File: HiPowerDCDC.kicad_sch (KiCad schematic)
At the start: 69 parts, among them J1 Conn_01x01, J2 Conn_01x01, J3 Conn_01x01, J4 Conn_01x01, J5 Conn_01x04, J6 Conn_01x02, Q1 WMJ38N60, Q2 WMJ38N60, SW1 SW_Push, SW2 SW_Push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

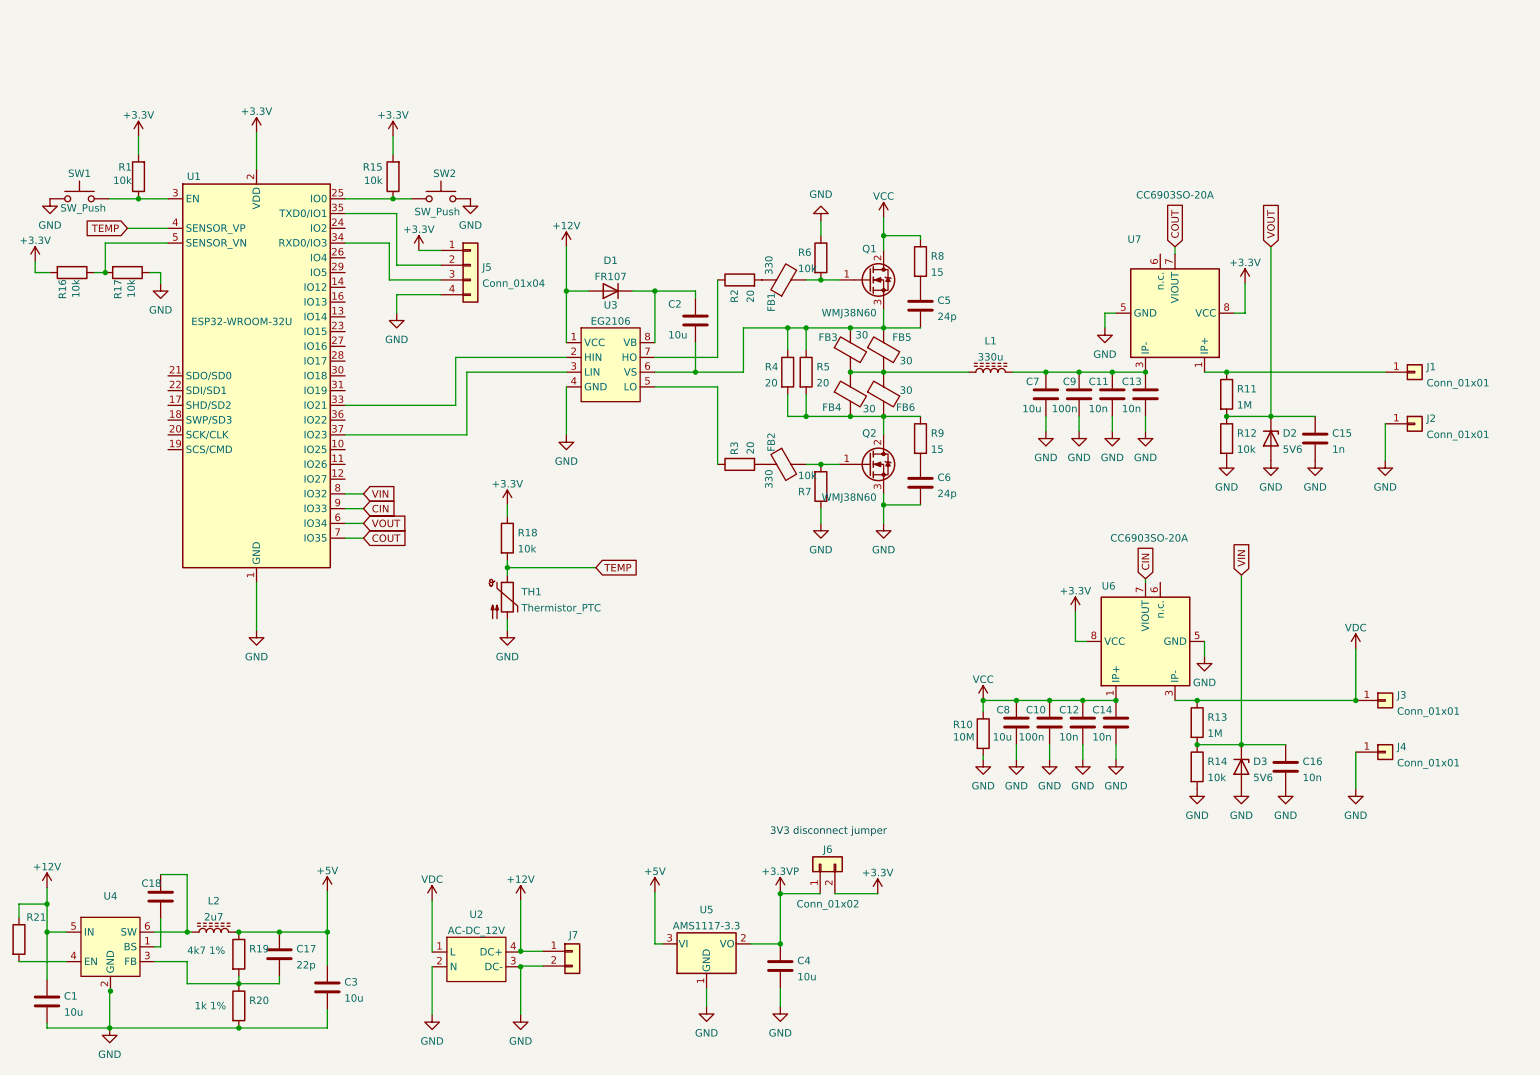
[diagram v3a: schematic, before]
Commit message: Increased DCDC inductor footprint
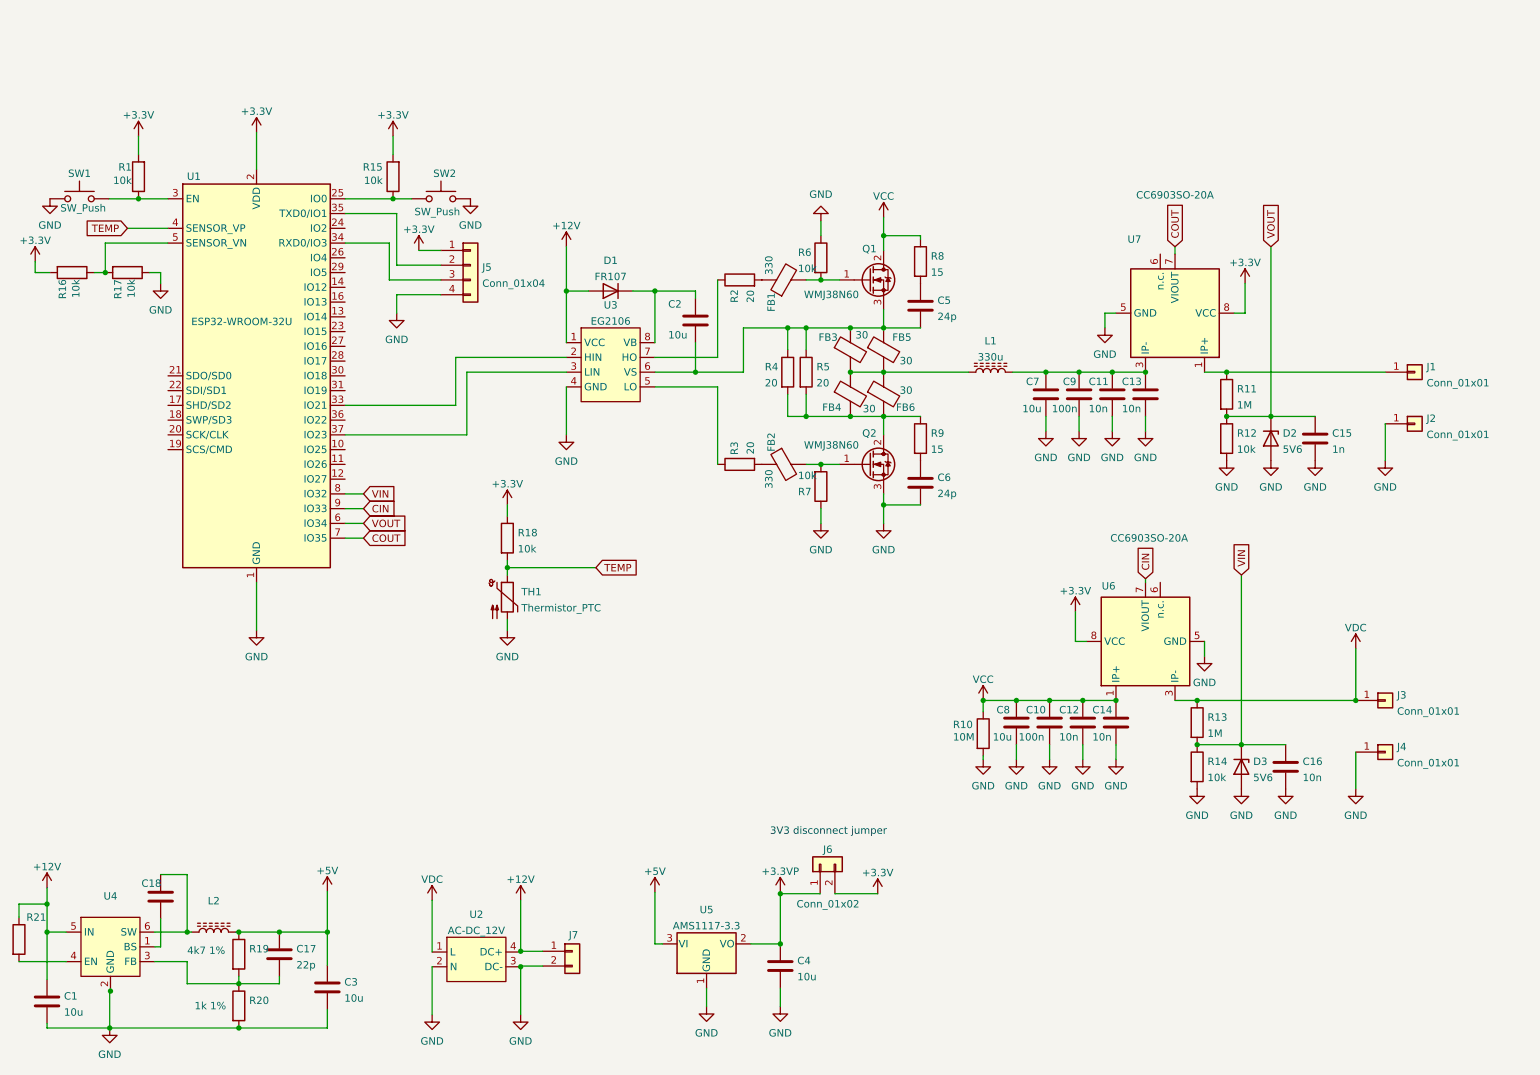
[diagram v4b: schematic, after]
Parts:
- L2: value 2u7 -> (none); footprint Inductor_SMD:L_1206_3216Metric -> (none)
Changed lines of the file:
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@@
       (effects (font (size 1.27 1.27)) (justify left))
     )
-    (property "Value" "WMJ38N60" (id 1) (at 153.1621 97.1166 0)
+    (property "Value" "WMJ38N60" (id 1) (at 150.114 88.138 0)
       (effects (font (size 1.27 1.27)) (justify left))
     )
@@
     (in_bom yes) (on_board yes) (fields_autoplaced)
     (property "Reference" "L2" (id 0) (at 48.514 166.5944 90))
-    (property "Value" "2u7" (id 1) (at 48.514 169.3695 90))
-    (property "Footprint" "Inductor_SMD:L_1206_3216Metric" (id 2) (at 48.514 171.958 0)
+    (property "Value" "" (id 1) (at 48.514 169.3695 90))
+    (property "Footprint" "" (id 2) (at 48.514 171.958 0)
       (effects (font (size 1.27 1.27)) hide)
     )
@@
       (effects (font (size 1.27 1.27)) (justify left))
     )
-    (property "Value" "WMJ38N60" (id 1) (at 153.1621 65.3666 0)
+    (property "Value" "WMJ38N60" (id 1) (at 150.114 62.23 0)
       (effects (font (size 1.27 1.27)) (justify left))
     )
@@
     )
     (path "/95159484-e5f5-4966-8d7a-72189e5ff978"
-      (reference "L2") (unit 1) (value "2u7") (footprint "Inductor_SMD:L_1206_3216Metric")
+      (reference "L2") (unit 1) (value "4u7") (footprint "Inductor_SMD:L_1210_3225Metric")
     )
     (path "/9f3445bc-88a2-4117-bce4-7aec366bd190"

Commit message: Finished PCB..then Laci started to complain :(
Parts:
- added D4, D5: FR107, Diode_SMD:D_SOD-123, symbol Device:D
- added J8: (no value), symbol Connector:Conn_01x01
- added J9: VDD_BP, Connector_PinSocket_2.54mm:PinSocket_1x01_P2.54mm_Vertical, symbol Connector:Conn_01x01
- C18: value (none) -> 22n; footprint (none) -> Capacitor_SMD:C_1206_3216Metric
- J7: value (none) -> 12V Fan
- L2: value (none) -> 4u7; footprint (none) -> Inductor_SMD:L_1210_3225Metric
- R21: value (none) -> 100k; footprint (none) -> Resistor_SMD:R_1206_3216Metric
- U4: value (none) -> SD8942; footprint (none) -> Package_TO_SOT_SMD:SOT-23-6
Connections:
- net +12V: now also U5.3 (VI)
- net +3.3VP: now also C17.1, C3.1, L2.2, R19.1
- net VDC: now also D4.2 (A); no longer U2.1 (L)
- net VDD: now reaches J1.1 (Pin_1), R11.1, U7.1 (IP+), U7.2 (IP+)
- net VDD: now also J9.1 (Pin_1)
- removed net +5V: C17.1, C3.1, L2.2, R19.1, U5.3 (VI)
- new net: D5.2 (A), J8.1 (Pin_1)
- new net: D4.1 (K), D5.1 (K), U2.1 (L)
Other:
- note added: "Bypass with a wire"
- note added: "Optional"
- moved on the sheet: J7, U2

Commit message: Laci, do you want me to re design the whole f*kin PCB?
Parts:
- added R23, R24: 330k, Resistor_SMD:R_1206_3216Metric, symbol Device:R
- added R25: (no value), symbol Device:R
- added R26: (no value), Resistor_SMD:R_1206_3216Metric, symbol Device:R
- J8: value (none) -> VDD_BP; footprint (none) -> Connector_PinSocket_2.54mm:PinSocket_1x01_P2.54mm_Vertical
- R10: value 10M -> (none); footprint Resistor_SMD:R_1812_4532Metric -> (none)
- R11: value 1M -> (none)
- R13: value 1M -> (none); footprint Resistor_SMD:R_1206_3216Metric -> (none)
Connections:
- net VDD: now also R25.1; no longer R11.1
- net VIN: now also R24.2; no longer R13.2
- net VOUT: now also R26.2; no longer R11.2
- new net: R13.2, R23.1
- new net: R23.2, R24.1
- new net: R11.1, R25.2
- new net: R11.2, R26.1
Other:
- moved on the sheet: C15, C16, D2, D3, J1, J2, R11, R12, R13, R14

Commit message: Finalized PCB
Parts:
- added C19, C20, C21: 1u, Capacitor_THT:C_Rect_L26.5mm_W11.5mm_P22.50mm_MKS4, symbol Device:C
- added F1: Fuse, Laci:Fuseholder_Schurter_0751.0505, symbol Device:Fuse
- added GD1: GDT_2Pin, HiPowerFP:CG2-350L, symbol Device:GDT_2Pin
- added J10: Conn_01x01, HiPowerFP:Keystone_7808, symbol Connector:Conn_01x01
- added RV1, RV2: V275LA20AP, Varistor:RV_Disc_D15.5mm_W3.9mm_P7.5mm, symbol Device:Varistor
- R10: value (none) -> 1M; footprint (none) -> Resistor_THT:R_Axial_DIN0207_L6.3mm_D2.5mm_P10.16mm_Horizontal
- R11, R26: value (none) -> 330k
- R13, R25: value (none) -> 330k; footprint (none) -> Resistor_SMD:R_1206_3216Metric
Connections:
- net GND: now also C20.2, C21.2, RV2.2; no longer C4.2
- net VDC: now also C19.1, C21.1, F1.1, RV1.1; no longer J3.1 (Pin_1)
- new net: GD1.2, RV1.2, RV2.1
- new net: F1.2, J3.1 (Pin_1)
- new net Earth: C19.2, C20.1, GD1.1, J10.1 (Pin_1)
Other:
- note added: "Input protection and filter"
- moved on the sheet: C10, C11, C12, C13, C14, C15, C16, C2, C5, C6, C7, C8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

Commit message: Added FW and fixed monor bugs
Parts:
- D2, D3: value 5V6 -> (none); footprint Diode_SMD:D_1206_3216Metric -> (none)
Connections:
- net GND: now also C4.2
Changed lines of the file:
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@@
     (pin "2")
+  )
+  (symbol (lib_id "power:GND") (at 146.05 184.785 0) (unit 1)
+    (in_bom yes) (on_board yes) (fields_autoplaced)
+    (property "Reference" "#PWR?" (id 0) (at 146.05 191.135 0)
+      (effects (font (size 1.27 1.27)) hide)
+    )
+    (property "Value" "GND" (id 1) (at 146.05 189.3476 0))
+    (property "Footprint" "" (id 2) (at 146.05 184.785 0)
+      (effects (font (size 1.27 1.27)) hide)
+    )
+    (property "Datasheet" "" (id 3) (at 146.05 184.785 0)
+      (effects (font (size 1.27 1.27)) hide)
+    )
+    (pin "1")
   )
   (symbol (lib_id "Connector:Conn_01x01") (at 257.175 121.285 0) (unit 1)
@@
       (effects (font (size 1.27 1.27)) (justify left))
     )
-    (property "Value" "5V6" (id 1) (at 195.0721 134.5816 90)
-      (effects (font (size 1.27 1.27)) (justify left))
-    )
-    (property "Footprint" "Diode_SMD:D_1206_3216Metric" (id 2) (at 193.04 132.715 0)
+    (property "Value" "" (id 1) (at 195.0721 134.5816 90)
+      (effects (font (size 1.27 1.27)) (justify left))
+    )
+    (property "Footprint" "" (id 2) (at 193.04 132.715 0)
       (effects (font (size 1.27 1.27)) hide)
     )
@@
       (effects (font (size 1.27 1.27)) (justify left))
     )
-    (property "Value" "5V6" (id 1) (at 236.3471 72.9866 90)
-      (effects (font (size 1.27 1.27)) (justify left))
-    )
-    (property "Footprint" "Diode_SMD:D_1206_3216Metric" (id 2) (at 234.315 71.12 0)
+    (property "Value" "" (id 1) (at 236.3471 72.9866 90)
+      (effects (font (size 1.27 1.27)) (justify left))
+    )
+    (property "Footprint" "" (id 2) (at 234.315 71.12 0)
       (effects (font (size 1.27 1.27)) hide)
     )
@@
       (reference "#PWR0160") (unit 1) (value "Earth") (footprint "")
     )
+    (path "/6726f8e4-8d42-46b9-981e-3ba2f7aae3a3"
+      (reference "#PWR?") (unit 1) (value "GND") (footprint "")
+    )
     (path "/f5b2acb3-5270-49b7-9759-e340f763a634"
       (reference "C1") (unit 1) (value "10u") (footprint "Capacitor_SMD:C_1206_3216Metric")
@@
     )
     (path "/efaadf6c-74aa-4770-bea2-28f4b6acc646"
-      (reference "D2") (unit 1) (value "5V6") (footprint "Diode_SMD:D_1206_3216Metric")
+      (reference "D2") (unit 1) (value "3V6") (footprint "Diode_SMD:D_1206_3216Metric")
     )
     (path "/86e58e79-f468-46ff-ada4-5f6163e175da"
-      (reference "D3") (unit 1) (value "5V6") (footprint "Diode_SMD:D_1206_3216Metric")
+      (reference "D3") (unit 1) (value "3V6") (footprint "Diode_SMD:D_1206_3216Metric")
     )
     (path "/7956388e-953c-44cd-9818-020b2e5e3f13"
